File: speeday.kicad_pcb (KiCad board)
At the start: 4 copper layers, 100 x 100 mm, 283 parts, among them IC1 LM3940IMP-3.3_NOPB, IC10 VNL5090N3-E, IC2 Trig Cond Socket, IC3 VNL5090N3-E, IC4 VNL5090N3-E, IC5 VNL5090N3-E, IC6 VNL5090N3-E, IC7 VNL5090N3-E, IC8 VNL5090N3-E, IC9 VNL5090N3-E, J1 Micro_SD_Card, J10 Conn_02x02_Counter_Clockwise, J11 Conn_02x02_Counter_Clockwise, J12 Conn_01x01, J13 Conn_01x01, J14 Conn_01x01, J15 Conn_01x01, J16 Conn_01x02, J17 Conn_01x02, J18 Conn_01x02, J19 Conn_01x02, J2 Conn_01x02, J20 Conn_01x04, J21 Conn_01x04, J22 Conn_01x04, J23 Conn_01x02, J24 Conn_01x02, J25 Conn_01x08, J26 Conn_01x08, J27 Conn_01x04, J3 Screw_Terminal_01x02, J4 Conn_02x02_Counter_Clockwise, J5 Conn_02x02_Counter_Clockwise, J6 Conn_02x02_Counter_Clockwise, J7 Conn_02x02_Counter_Clockwise, J8 Conn_02x02_Counter_Clockwise, J9 Conn_02x02_Counter_Clockwise, P1 USB_C_Plug_USB2.0, Q1 SSM3K357R, Q2 SSM3K357R, Q3 SSM3K357R, Q4 SSM3K357R, SW1 SW_DIP_x01, SW2 SW_DIP_x01, U1 STM32F407VGTx, U10 SP720, U11 MCP2551-I-SN, U12 IXDN602, U13 IXDN602, U14 LM2940S-5.0/NOPB, U2 MCP6004, U3 MCP6002-xMS, U4 MCP6004, U5 MCP6004, U6 TXB0108PW, U7 TXB0108PW, U8 W25Q16JVSS, U9 MPX4250, Y1 Crystal_GND23

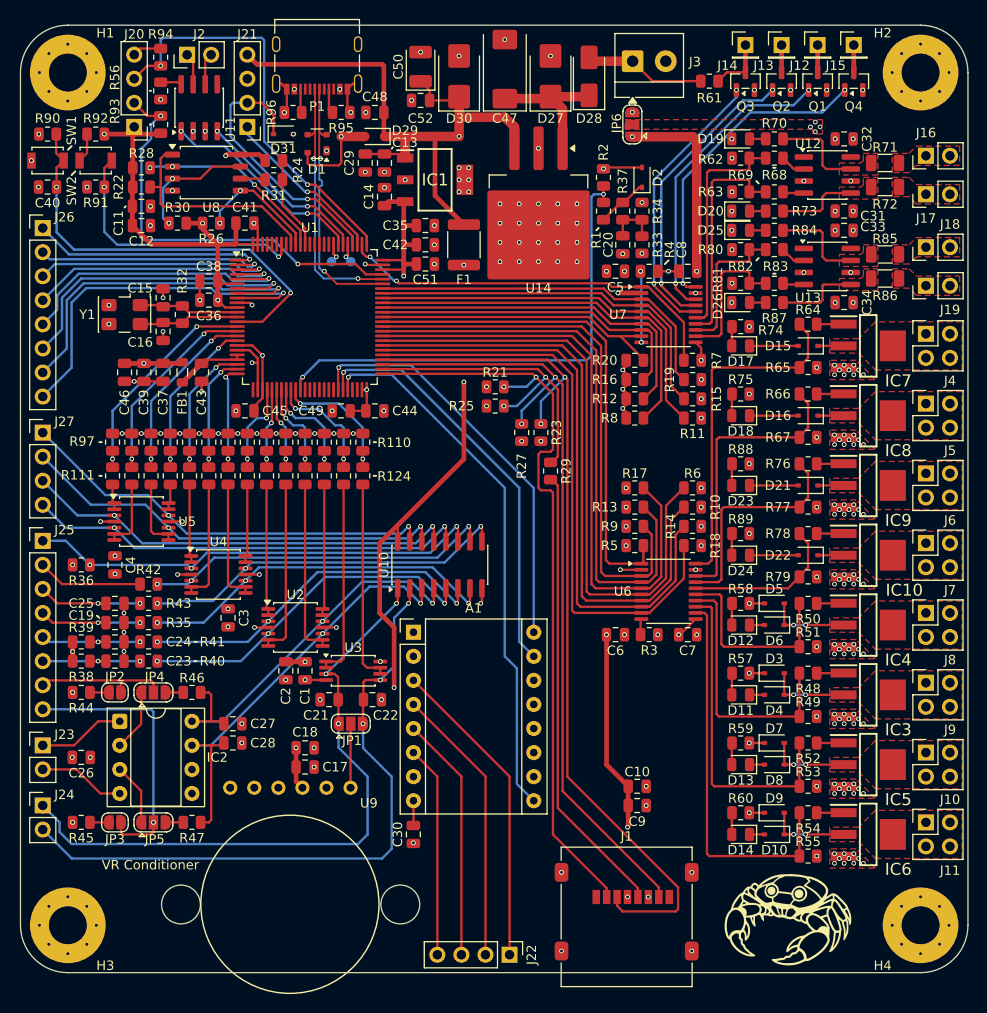
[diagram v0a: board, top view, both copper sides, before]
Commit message: Change power layout, add low frequency crystal
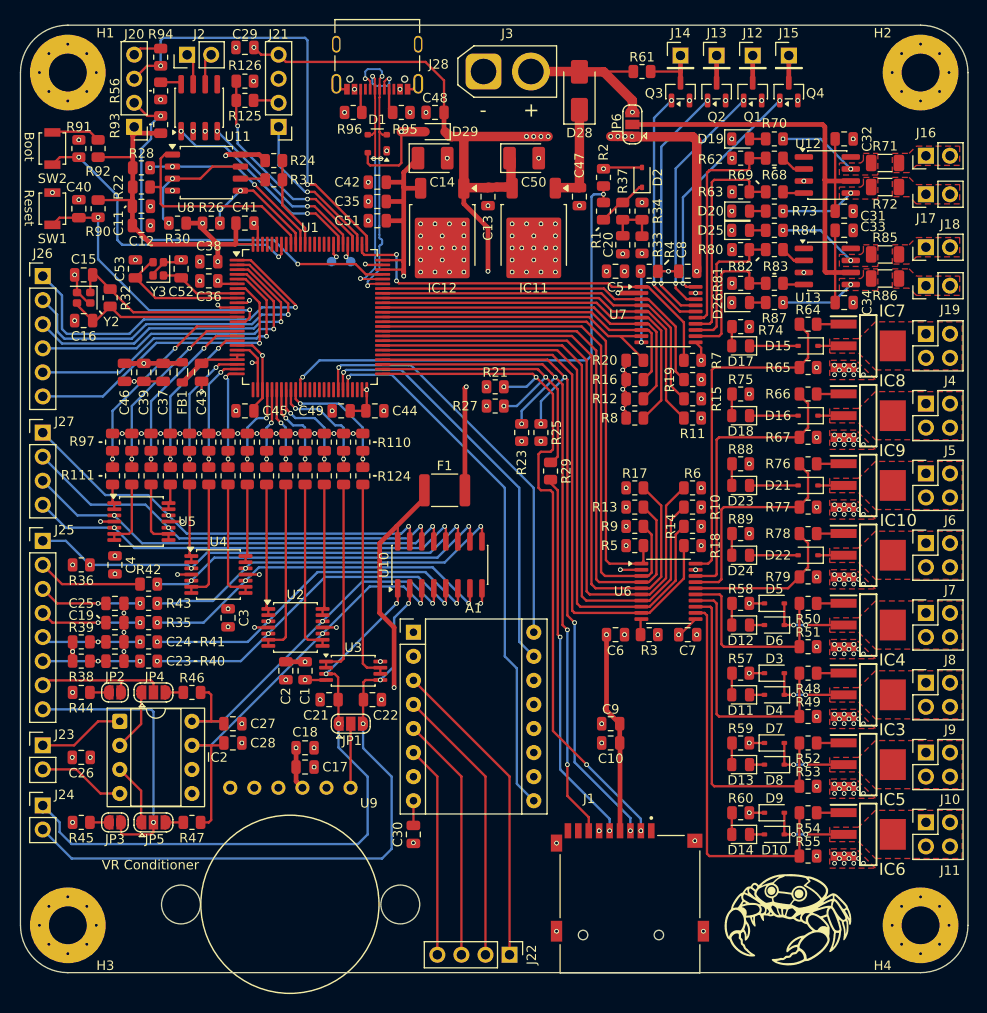
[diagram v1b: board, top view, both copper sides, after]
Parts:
- removed D27, D30: D_TVS, Diode_SMD:D_SMB
- removed D31: D_Zener, Diode_SMD:D_SOD-323
- removed IC1: LM3940IMP-3.3_NOPB, Misc:SOT230P700X180-4N
- removed P1: USB_C_Plug_USB2.0, Connector_USB:USB_C_Receptacle_Palconn_UTC16-G
- removed U14: LM2940S-5.0/NOPB, IC_Automotive:TO-263-3_TabPin2-Clean
- removed Y1: Crystal_GND23, Crystal:Crystal_SMD_5032-4Pin_5.0x3.2mm
- added C53: 12pF, Capacitor_SMD:C_0805_2012Metric, F.Cu at (32.1, 45.7)
- added IC11: LD29150DT50R, Package_TO_SOT_SMD:TO-252-2, F.Cu at (74.2, 42.2)
- added IC12: LD29150DT33R, Package_TO_SOT_SMD:TO-252-2, F.Cu at (64.5, 42.3)
- added J28: 12402012E212A, Misc:AMPHENOL_12402012E212A, F.Cu at (57.7, 22.0)
- added R125: 2k, Resistor_SMD:R_0805_2012Metric, F.Cu at (43.7, 27.9)
- added R126: 1k, Resistor_SMD:R_0805_2012Metric, F.Cu at (43.7, 25.9)
- added Y2: Crystal_GND24, Crystal:Crystal_SMD_2016-4Pin_2.0x1.6mm, F.Cu at (26.7, 48.8)
- added Y3: Crystal_GND24, Crystal:Crystal_SMD_2016-4Pin_2.0x1.6mm, F.Cu at (34.5, 45.7)
- C10, C12, C30: value 22µF -> 22uF
- C13: value 470pF -> 330nF
- C14: value 33µF -> 10uF; footprint Capacitor_SMD:C_0805_2012Metric -> Capacitor_Tantalum_SMD:CP_EIA-3528-12_Kemet-T
- C31, C33: value 0.1uF -> 100nF
- C35: value 10µ -> 10uF
- C36, C38, C41, C42, C44, C45, C46: value 100n -> 100nF
- C37: value 10n -> 10nF
- C39, C43: value 1µ -> 1uF
- C47: value 470nF -> 330nF; footprint Capacitor_Tantalum_SMD:CP_EIA-7343-31_Kemet-D -> Capacitor_SMD:C_0805_2012Metric
- C49, C51: value 2.2µ -> 2.2uF
- C50: value 47uF -> 10uF; footprint Capacitor_Tantalum_SMD:CP_EIA-3528-21_Kemet-B -> Capacitor_Tantalum_SMD:CP_EIA-3528-12_Kemet-T
- C52: value 100nF -> 12pF
- J1: value Micro_SD_Card -> MSD-4-A; footprint Connector_Card:microSD_HC_Molex_47219-2001 -> Misc:CUI_MSD-4-A
- J26: value Conn_01x08 -> Conn_01x06; footprint Connector_PinHeader_2.54mm:PinHeader_1x08_P2.54mm_Vertical -> Connector_PinHeader_2.54mm:PinHeader_1x06_P2.54mm_Vertical
- J3: value Screw_Terminal_01x02 -> Conn_01x02; footprint TerminalBlock_MetzConnect:TerminalBlock_MetzConnect_Type059_RT06302HBWC_1x02_P3.50mm_Horizontal -> Connector_AMASS:AMASS_XT30U-F_1x02_P5.0mm_Vertical
- R3, R4: value R -> 1k
- R56: value 4k7 -> 4.7k
- moved C52 30.9 mm to (37.0, 45.7), turned to 90 degrees
- moved F1 26.0 mm to (64.8, 69.1), turned to 180 degrees
- moved C29 17.6 mm to (43.7, 22.4), turned to 0 degrees
- moved J3 15.8 mm to (68.9, 24.9)
- moved C47 15.6 mm to (79.0, 38.1), turned to -90 degrees
- moved C50 14.6 mm to (73.2, 34.0), turned to 0 degrees
- moved C13 11.5 mm to (69.3, 38.1), turned to -90 degrees
- moved R90 9.51 mm to (28.2, 39.4), turned to -90 degrees
- moved C9 9.08 mm to (82.3, 93.7), turned to 0 degrees
- moved C15 8.72 mm to (26.7, 46.4), turned to 180 degrees
- moved C16 8.46 mm to (26.7, 51.2), turned to 180 degrees
- moved C42 8.33 mm to (57.7, 36.6), turned to 180 degrees
- moved R32 7.82 mm to (29.5, 48.8)
- moved NT1 7.34 mm to (70.7, 37.1), turned to 0 degrees
- moved R61 7.18 mm to (85.6, 24.9)
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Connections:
- net MCU-OSC-IN renamed MCU-HSE-OSC-IN
- net MCU-OSC-OUT renamed MCU-HSE-OSC-OUT
- C13 pad 1: GND -> +5V
- C13 pad 2: +5V -> GND
- C14 pad 1: GND -> +3.3V
- C14 pad 2: +3.3V -> GND
- C52 pad 1: 5V-REGULATOR -> MCU-LSE-OSC-IN
- J21 pad 2: MCU-UART-BT-RX -> Net-(J21-Pin_2)
- J3 pad 1: VBAT -> GND
- J3 pad 2: GND -> VBAT
- R23 pad 1: MCU-SPI-SD-MOSI -> MCU-SPI-SD-MISO
- R25 pad 1: MCU-SPI-SD-CLK -> MCU-SPI-SD-MOSI
- R27 pad 1: MCU-SPI-SD-MISO -> MCU-SPI-SD-CLK
- R95 pad 1: Net-(P1-CC) -> GND
- R95 pad 2: GND -> Net-(J28-CC1_A)
- U1 pad 8: MCU-EXTRA-GPIO-7-D -> MCU-LSE-OSC-IN
- U1 pad 9: MCU-EXTRA-GPIO-8-D -> MCU-LSE-OSC-OUT
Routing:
- net Vdrive: track 0.00 -> 56.6 mm, vias 10 -> 0
- net MCU-EXTRA-GPIO-8-D: track 39.6 -> 0.00 mm, vias 1 -> 0
- net MCU-EXTRA-GPIO-7-D: track 36.7 -> 0.00 mm, vias 1 -> 0
- net +5V: track 239.3 -> 268.8 mm, vias 15 -> 24
- net +5VA: track 127.7 -> 102.2 mm, vias 8 -> 6
- net MCU-SPI-SD-MOSI: track 94.8 -> 76.7 mm, vias 2 -> 4
- net MCU-EXTRA-GPIO-1-D: track 24.6 -> 40.8 mm
- net MCU_RESET: track 45.4 -> 30.2 mm
- net MCU-LSE-OSC-OUT: track 0.00 -> 14.2 mm
- net 5V-REGULATOR: track 17.3 -> 4.04 mm
- net MCU-EXTRA-GPIO-2-D: track 25.0 -> 37.9 mm
- net MCU-SPI-SD-MISO: track 84.6 -> 74.5 mm, vias 2 -> 4
- net MCU-EXTRA-GPIO-3-D: track 26.1 -> 35.0 mm
- net MCU-LSE-OSC-IN: track 0.00 -> 8.56 mm
- net LC-TRIG: track 33.4 -> 25.0 mm
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- removed copper zone on In2.Cu, net 5V-USB
- removed copper zone on F.Cu, net Vdrive
- removed copper zone on In2.Cu, net Vdrive
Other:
- rule pad_to_mask_clearance: 0.051 -> 0
- board text added: "Boot"
- board text added: "Reset"
